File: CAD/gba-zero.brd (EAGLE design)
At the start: 130.7 x 72.9 mm, 57 parts, among them J1 SWTCHCRFT_3.5JACK5-JACK-SMD, P1 50_PIN_CON, P3 LINK_CONNECTOR, Q1 BSS138, U1 APX803, U2 NC7WZ16, U3 74LVC2G02, U4 74LVC3G04, U5 LM4875, U6 RPI-ZEROSMD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

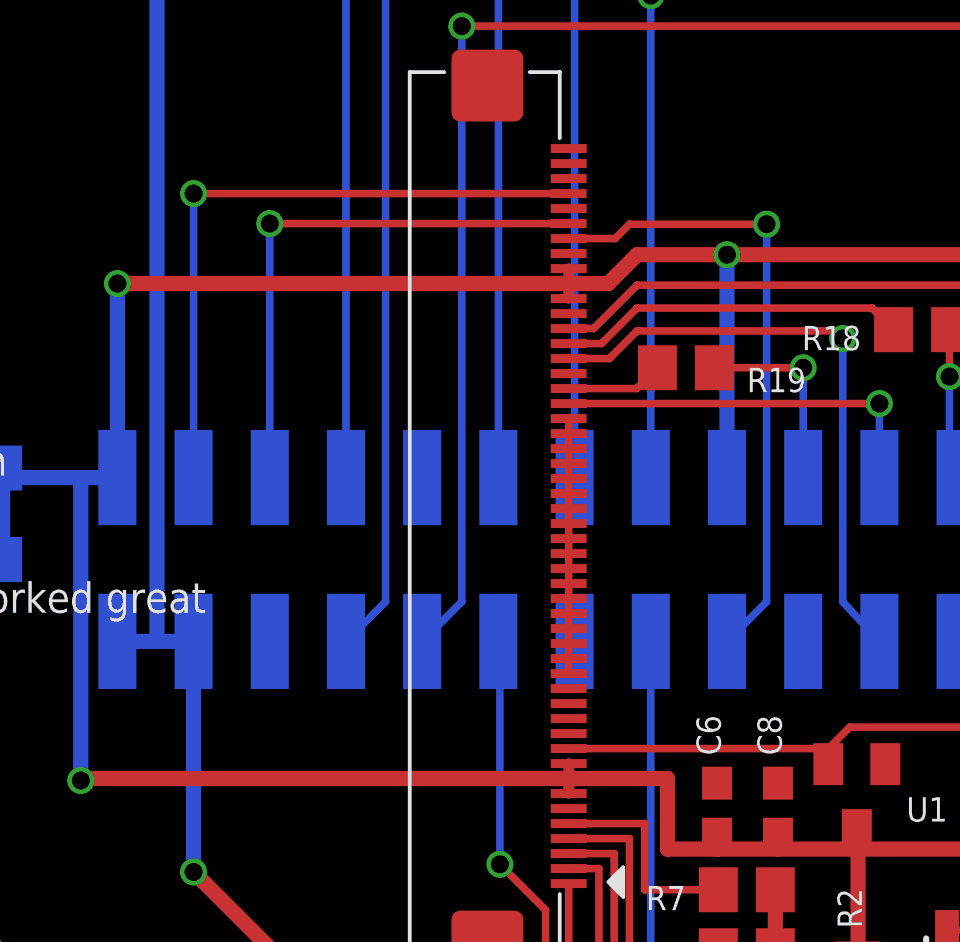
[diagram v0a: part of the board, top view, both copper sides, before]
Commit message: Rerouted display control lines Added missing connection between pins 10 & 47 on the display connector
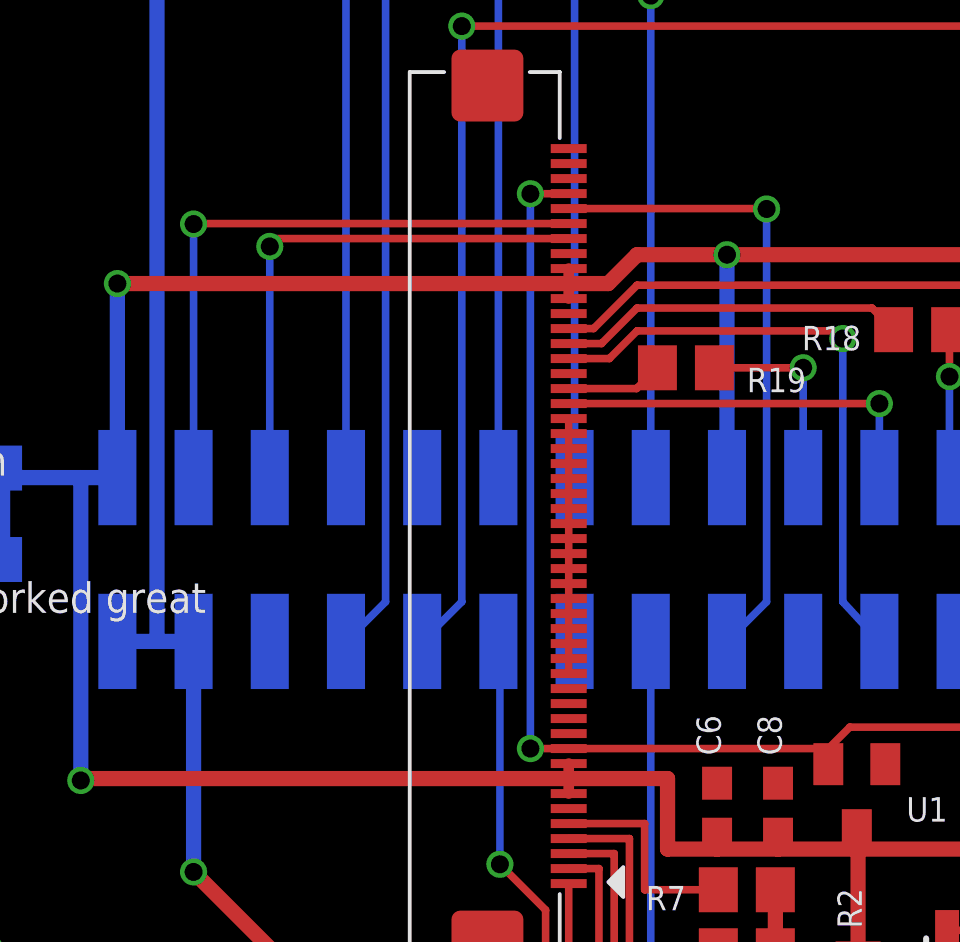
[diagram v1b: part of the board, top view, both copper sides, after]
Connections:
- net RT_INT: now also P1.46; no longer P1.44
- net SCL: now also P1.44; no longer P1.45
- net SDA: now also P1.45; no longer P1.47
- net TFT_RST: now also P1.47
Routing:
- net TFT_RST: track 16.5 -> 37.5 mm, vias 0 -> 2
- net SDA: track 22.0 -> 21.0 mm
- net SCL: track 18.4 -> 17.9 mm
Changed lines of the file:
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@@
 <wire x1="71.259740625" y1="33.02" x2="67.287559375" y2="33.02" width="0.254" layer="1"/>
 <wire x1="67.287559375" y1="33.02" x2="66.573359375" y2="32.3058" width="0.254" layer="1"/>
+<contactref element="P1" pad="47"/>
+<via x="56.642" y="50.8" extent="1-16" drill="0.6" shape="square"/>
+<wire x1="56.642" y1="50.8" x2="56.642" y2="32.3058" width="0.254" layer="16"/>
+<via x="56.642" y="32.3058" extent="1-16" drill="0.6" shape="square"/>
+<wire x1="56.642" y1="32.3058" x2="57.9204" y2="32.3058" width="0.254" layer="1"/>
+<wire x1="57.9204" y1="50.8058" x2="57.9204" y2="50.8" width="0.254" layer="1"/>
+<wire x1="57.9204" y1="50.8" x2="56.642" y2="50.8" width="0.254" layer="1"/>
 </signal>
 <signal name="RT_INT">
-<contactref element="P1" pad="44"/>
 <contactref element="U6" pad="18"/>
 <wire x1="63.1952" y1="35.8775" x2="64.516" y2="37.1983" width="0.254" layer="16"/>
-<wire x1="64.516" y1="37.1983" x2="64.516" y2="49.784" width="0.254" layer="16"/>
-<via x="64.516" y="49.784" extent="1-16" drill="0.6" shape="square"/>
-<wire x1="64.516" y1="49.784" x2="59.944" y2="49.784" width="0.254" layer="1"/>
-<wire x1="59.944" y1="49.784" x2="59.4658" y2="49.3058" width="0.254" layer="1"/>
-<wire x1="59.4658" y1="49.3058" x2="57.9204" y2="49.3058" width="0.254" layer="1"/>
+<wire x1="64.516" y1="37.1983" x2="64.516" y2="50.292" width="0.254" layer="16"/>
+<contactref element="P1" pad="46"/>
+<wire x1="57.9204" y1="50.3058" x2="64.516" y2="50.3058" width="0.254" layer="1"/>
+<wire x1="64.516" y1="50.3058" x2="64.516" y2="50.292" width="0.254" layer="1"/>
+<via x="64.516" y="50.292" extent="1-16" drill="0.6" shape="square"/>
 </signal>
 <signal name="SCLK">
@@
 </signal>
 <signal name="SDA">
-<contactref element="P1" pad="47"/>
 <contactref element="U6" pad="3"/>
-<wire x1="57.9204" y1="50.8058" x2="45.4152" y2="50.8058" width="0.254" layer="1"/>
-<via x="45.4152" y="50.8058" extent="1-16" drill="0.6" shape="square"/>
-<wire x1="45.4152" y1="50.8058" x2="45.4152" y2="41.3385" width="0.254" layer="16"/>
+<via x="45.4152" y="49.7898" extent="1-16" drill="0.6" shape="square"/>
+<wire x1="45.4152" y1="49.7898" x2="45.4152" y2="41.3385" width="0.254" layer="16"/>
+<contactref element="P1" pad="45"/>
+<wire x1="57.9204" y1="49.8058" x2="45.4152" y2="49.8058" width="0.254" layer="1"/>
+<wire x1="45.4152" y1="49.8058" x2="45.4152" y2="49.7898" width="0.254" layer="1"/>
 </signal>
 <signal name="SCL">
-<contactref element="P1" pad="45"/>
 <contactref element="U6" pad="5"/>
-<wire x1="57.9204" y1="49.8058" x2="47.9552" y2="49.8058" width="0.254" layer="1"/>
-<via x="47.9552" y="49.8058" extent="1-16" drill="0.6" shape="square"/>
-<wire x1="47.9552" y1="49.8058" x2="47.9552" y2="41.3385" width="0.254" layer="16"/>
+<via x="47.9552" y="49.0438" extent="1-16" drill="0.6" shape="square"/>
+<wire x1="47.9552" y1="49.0438" x2="47.9552" y2="41.3385" width="0.254" layer="16"/>
+<contactref element="P1" pad="44"/>
+<wire x1="57.9204" y1="49.3058" x2="47.9552" y2="49.3058" width="0.254" layer="1"/>
+<wire x1="47.9552" y1="49.3058" x2="47.9552" y2="49.0438" width="0.254" layer="1"/>
 </signal>
 <signal name="3.3V">

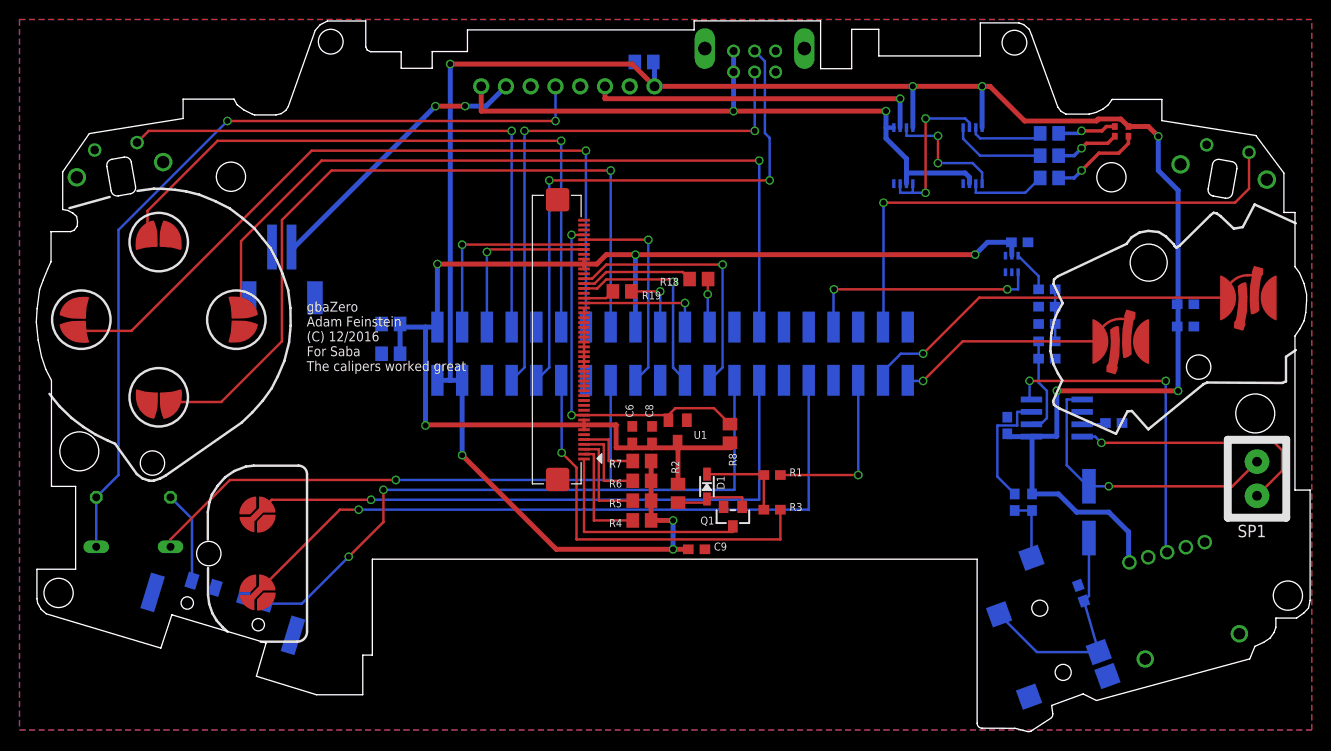
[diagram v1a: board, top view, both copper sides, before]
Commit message: Shifted display hardware, added more space in the battery area
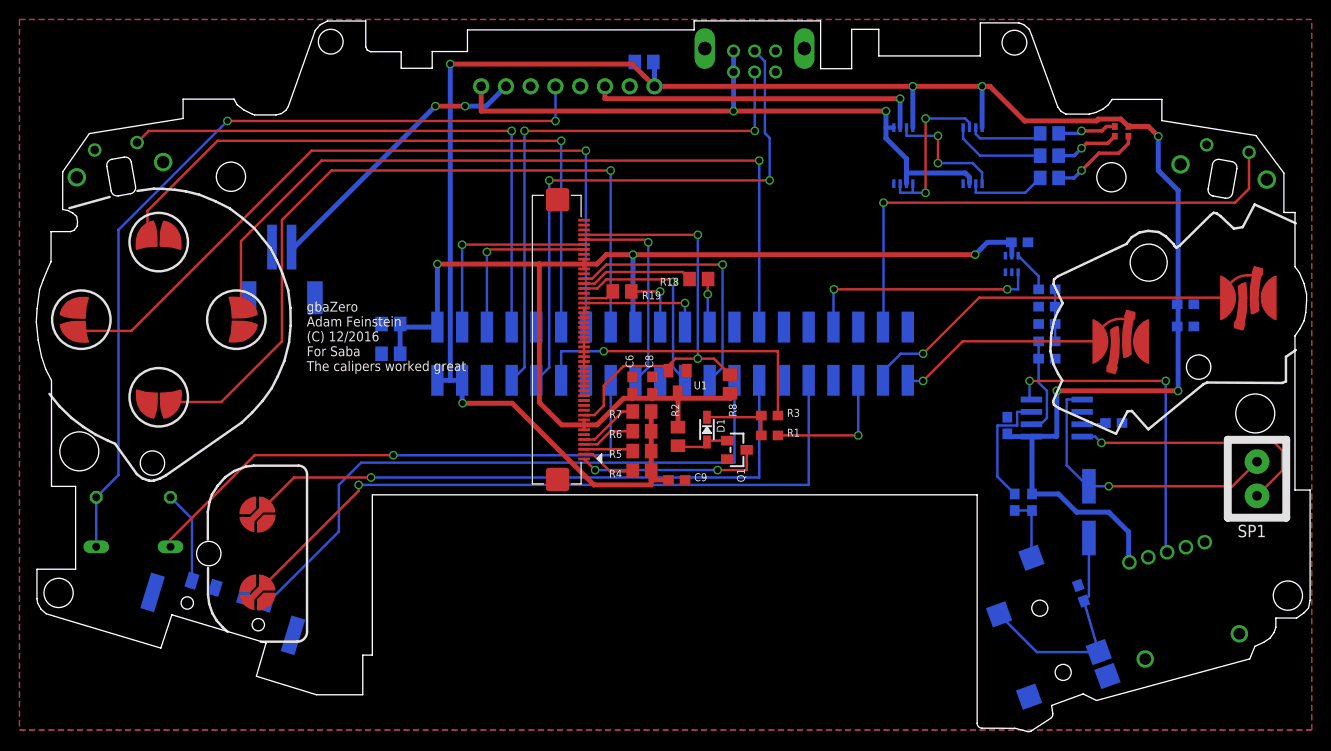
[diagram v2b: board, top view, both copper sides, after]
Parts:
- moved R3 9.66 mm to (77.0, 32.3)
- moved C9 7.40 mm to (67.4, 25.7)
- moved Q1 6.86 mm to (73.6, 28.7), turned to 270 degrees
- moved D1 5.84 mm to (70.5, 30.8)
- moved R2 5.84 mm to (67.6, 30.1)
- moved R4 5.08 mm to (63.9, 26.6)
- moved R5 5.08 mm to (63.9, 28.6)
- moved R6 5.08 mm to (63.9, 30.6)
- moved R8 5.08 mm to (72.9, 35.5)
- moved C6 5.08 mm to (62.9, 35.4)
- moved C8 5.08 mm to (64.9, 35.4)
- moved R7 5.08 mm to (63.9, 32.7)
- moved U1 5.08 mm to (67.5, 35.8)
- moved R1 4.07 mm to (77.0, 30.2)
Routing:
- net +5V: track 238.4 -> 226.7 mm, vias 9 -> 7
- net BKLT_PWM: track 40.9 -> 31.8 mm
- net 3.3V: track 133.9 -> 125.3 mm, vias 4 -> 3
- net TFT_RST: track 37.5 -> 44.2 mm
- net N$10: track 11.9 -> 5.75 mm
- net N$4: track 10.3 -> 5.07 mm
- net N$1: track 23.3 -> 19.2 mm, vias 0 -> 2
- net BKLT: track 17.7 -> 13.9 mm
- net N$3: track 8.73 -> 5.54 mm
- net N$7: track 8.11 -> 5.83 mm
- net N$6: track 9.48 -> 7.78 mm
- net PWR_EN_RPI: track 58.7 -> 57.2 mm
- net BTN_STR: track 64.4 -> 63.1 mm
- net BTN_SEL: track 73.4 -> 72.3 mm
- net N$2: track 7.19 -> 6.18 mm
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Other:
- outline, holes or cut-outs redrawn

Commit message: Added diodes to power LED logic by USB & regulated 5V Cleaned up layout
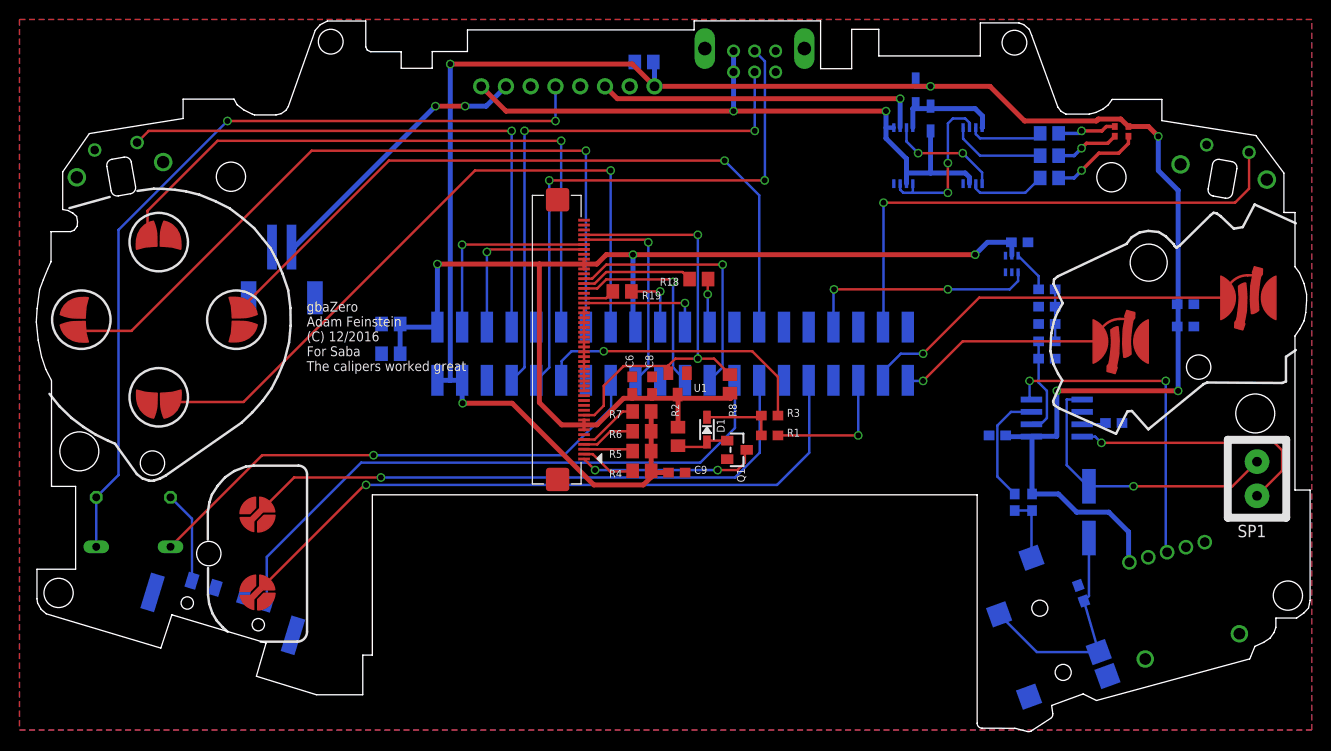
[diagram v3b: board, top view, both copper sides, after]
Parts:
- added D4, D5: 1N4148, microbuilder:SOD-323
- moved C7 1.44 mm to (100.3, 30.2), turned to 180 degrees
- moved C9 0.76 mm to (67.4, 26.4)
- moved U1 0.25 mm to (67.5, 35.5)
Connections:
- new net N$19: D4.C, D5.C, U3.8, U4.8
- net +5V: now also D4.A; no longer U3.8, U4.8
- net USB: now also D5.A
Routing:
- net N$19: track 0.00 -> 11.4 mm
- net BTN_D: track 79.1 -> 71.8 mm
- net +5V: track 226.7 -> 220.0 mm, vias 7 -> 6
- net BTN_R: track 80.6 -> 74.4 mm
- net PWR_EN_RPI: track 57.2 -> 54.0 mm
- net USB: track 66.7 -> 69.5 mm
- net BTN_SEL: track 72.3 -> 70.1 mm
- net BKLT_PWM: track 31.8 -> 29.7 mm
- net PWR_SW_SEN: track 65.2 -> 63.2 mm
- net BTN_STR: track 63.1 -> 61.6 mm
- net N$15: track 12.9 -> 11.6 mm
- net SENSE: track 12.7 -> 11.8 mm
- net LBO: track 34.5 -> 33.8 mm
- net RXD: track 57.6 -> 56.9 mm
- net N$1: track 19.2 -> 18.7 mm
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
